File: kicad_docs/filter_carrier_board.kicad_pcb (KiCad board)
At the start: 2 copper layers, 58.4 x 99.1 mm, 30 parts, among them J1 cv_in, J10 PJ301M-12, J2 signal_in, J3 signal_out, J4 power_and_rez_cv_in, J5 PJ301M-12, J6 PJ301M-12, J7 PJ301M-12, J8 PJ301M-12, J9 power_in, U1 TL072

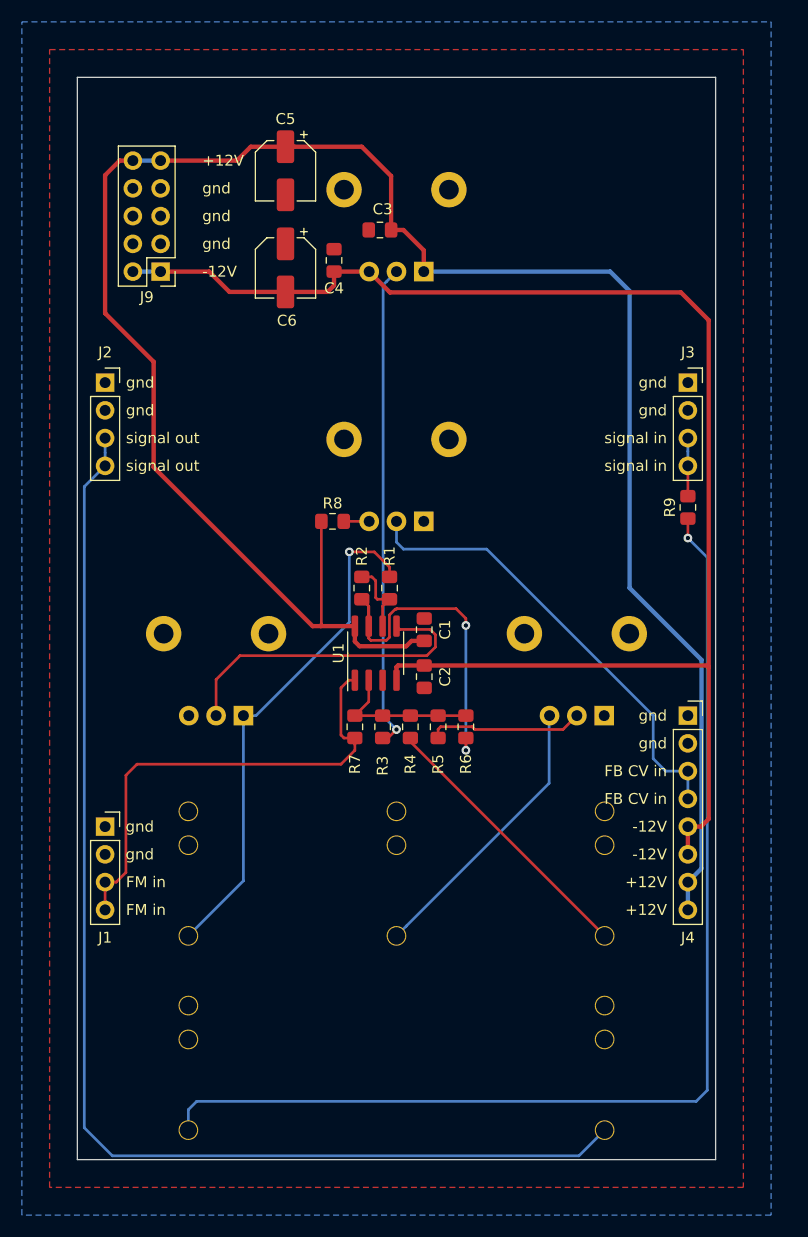
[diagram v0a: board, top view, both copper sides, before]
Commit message: route pcb traces away from pot footprints
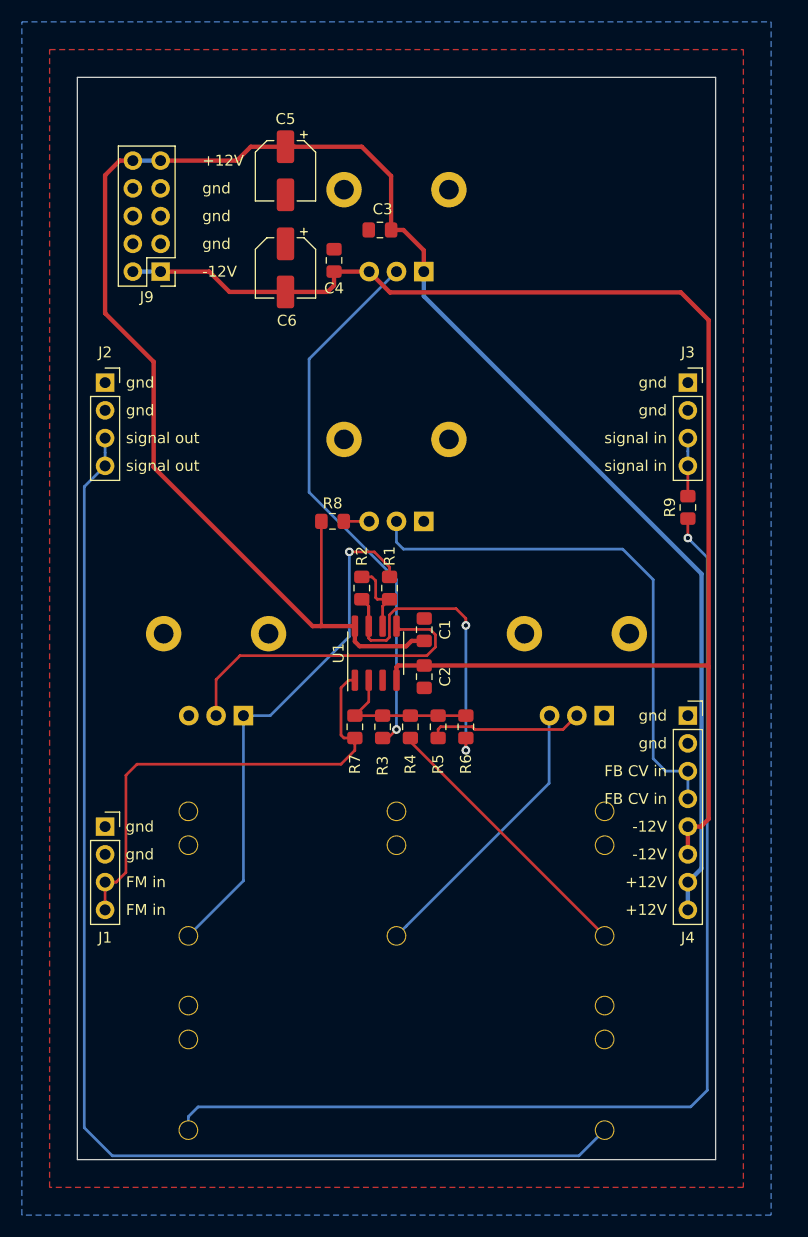
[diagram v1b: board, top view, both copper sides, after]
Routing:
- net +12V: track 191.1 -> 181.1 mm
- net Net-(J4-Pad3): track 42.1 -> 49.4 mm
- net Net-(R3-Pad2): track 44.5 -> 50.1 mm
- net Net-(J8-Pad3): track 47.1 -> 47.8 mm
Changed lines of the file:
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@@
     (thickness 1.6)
     (drawings 44)
-    (tracks 161)
+    (tracks 159)
     (zones 0)
     (modules 30)
@@
   (segment (start 105.41 68.58) (end 109.855 73.025) (width 0.4) (layer F.Cu) (net 1))
   (segment (start 109.855 82.677) (end 124.398 97.22) (width 0.4) (layer F.Cu) (net 1))
-  (segment (start 153.416 66.548) (end 151.638 64.77) (width 0.4) (layer B.Cu) (net 1))
-  (segment (start 153.416 93.726) (end 153.416 66.548) (width 0.4) (layer B.Cu) (net 1))
-  (segment (start 151.638 64.77) (end 134.58 64.77) (width 0.4) (layer B.Cu) (net 1))
-  (segment (start 160.000001 100.310001) (end 153.416 93.726) (width 0.4) (layer B.Cu) (net 1))
+  (segment (start 134.58 67.016) (end 134.58 64.77) (width 0.4) (layer B.Cu) (net 1))
+  (segment (start 160.000001 92.436001) (end 134.58 67.016) (width 0.4) (layer B.Cu) (net 1))
   (segment (start 158.75 120.65) (end 160.000001 119.399999) (width 0.4) (layer B.Cu) (net 1))
-  (segment (start 160.000001 119.399999) (end 160.000001 100.310001) (width 0.4) (layer B.Cu) (net 1))
+  (segment (start 160.000001 119.399999) (end 160.000001 92.436001) (width 0.4) (layer B.Cu) (net 1))
   (segment (start 158.75 118.11) (end 158.75 115.57) (width 0.4) (layer F.Cu) (net 3))
   (segment (start 158.75 115.57) (end 159.952081 115.57) (width 0.4) (layer F.Cu) (net 3))
@@
   (via (at 158.75 89.154) (size 0.8) (drill 0.4) (layers F.Cu B.Cu) (net 6))
   (segment (start 158.75 87.376) (end 158.75 89.154) (width 0.25) (layer F.Cu) (net 6))
-  (segment (start 159.512 140.716) (end 113.792 140.716) (width 0.25) (layer B.Cu) (net 6))
-  (segment (start 160.525011 139.702989) (end 159.512 140.716) (width 0.25) (layer B.Cu) (net 6))
-  (segment (start 113.792 140.716) (end 113.03 141.478) (width 0.25) (layer B.Cu) (net 6))
+  (segment (start 113.03 142.113) (end 113.03 143.35) (width 0.25) (layer B.Cu) (net 6))
+  (segment (start 159.004 141.224) (end 113.919 141.224) (width 0.25) (layer B.Cu) (net 6))
+  (segment (start 113.919 141.224) (end 113.03 142.113) (width 0.25) (layer B.Cu) (net 6))
+  (segment (start 160.525011 139.702989) (end 159.004 141.224) (width 0.25) (layer B.Cu) (net 6))
   (segment (start 158.75 89.154) (end 160.525011 90.929011) (width 0.25) (layer B.Cu) (net 6))
-  (segment (start 113.03 141.478) (end 113.03 143.35) (width 0.25) (layer B.Cu) (net 6))
   (segment (start 160.525011 90.929011) (end 160.525011 139.702989) (width 0.25) (layer B.Cu) (net 6))
-  (segment (start 158.75 81.212081) (end 158.75 82.55) (width 0.25) (layer B.Cu) (net 19))
-  (segment (start 158.75 80.01) (end 158.75 81.212081) (width 0.25) (layer B.Cu) (net 19))
   (segment (start 158.75 113.03) (end 158.75 110.49) (width 0.25) (layer B.Cu) (net 7))
+  (segment (start 132.08 89.535) (end 132.715 90.17) (width 0.25) (layer B.Cu) (net 7))
   (segment (start 156.718 110.49) (end 158.75 110.49) (width 0.25) (layer B.Cu) (net 7))
-  (segment (start 132.08 89.535) (end 132.715 90.17) (width 0.25) (layer B.Cu) (net 7))
   (segment (start 132.08 87.63) (end 132.08 89.535) (width 0.25) (layer B.Cu) (net 7))
-  (segment (start 155.575 105.41) (end 155.575 109.347) (width 0.25) (layer B.Cu) (net 7))
-  (segment (start 132.715 90.17) (end 140.335 90.17) (width 0.25) (layer B.Cu) (net 7))
-  (segment (start 140.335 90.17) (end 155.575 105.41) (width 0.25) (layer B.Cu) (net 7))
+  (segment (start 132.715 90.17) (end 152.781 90.17) (width 0.25) (layer B.Cu) (net 7))
+  (segment (start 155.575 92.964) (end 155.575 109.347) (width 0.25) (layer B.Cu) (net 7))
+  (segment (start 152.781 90.17) (end 155.575 92.964) (width 0.25) (layer B.Cu) (net 7))
   (segment (start 155.575 109.347) (end 156.718 110.49) (width 0.25) (layer B.Cu) (net 7))
   (segment (start 133.35 107.79) (end 133.35 107.46) (width 0.25) (layer F.Cu) (net 8))
@@
   (segment (start 118.07 120.53) (end 113.03 125.57) (width 0.25) (layer B.Cu) (net 10))
   (segment (start 118.07 105.41) (end 118.07 120.53) (width 0.25) (layer B.Cu) (net 10))
-  (segment (start 119.22 105.41) (end 118.07 105.41) (width 0.25) (layer B.Cu) (net 10))
-  (segment (start 127.762 96.868) (end 119.22 105.41) (width 0.25) (layer B.Cu) (net 10))
-  (segment (start 127.762 90.424) (end 127.762 96.868) (width 0.25) (layer B.Cu) (net 10))
   (via (at 127.762 90.424) (size 0.8) (drill 0.4) (layers F.Cu B.Cu) (net 10))
   (segment (start 130.048 90.424) (end 127.762 90.424) (width 0.25) (layer F.Cu) (net 10))
   (segment (start 131.445 92.71) (end 131.445 91.821) (width 0.25) (layer F.Cu) (net 10))
   (segment (start 131.445 91.821) (end 130.048 90.424) (width 0.25) (layer F.Cu) (net 10))
+  (segment (start 120.523 105.41) (end 118.07 105.41) (width 0.25) (layer B.Cu) (net 10))
+  (segment (start 127.762 90.424) (end 127.762 98.171) (width 0.25) (layer B.Cu) (net 10))
+  (segment (start 127.762 98.171) (end 120.523 105.41) (width 0.25) (layer B.Cu) (net 10))
   (segment (start 130.81 95.395) (end 131.445 94.76) (width 0.25) (layer F.Cu) (net 12))
   (segment (start 130.81 97.22) (end 130.81 95.395) (width 0.25) (layer F.Cu) (net 12))
@@
   (segment (start 137.52999 95.61999) (end 132.12002 95.61999) (width 0.25) (layer F.Cu) (net 13))
   (segment (start 132.12002 95.61999) (end 132.08 95.66001) (width 0.25) (layer F.Cu) (net 13))
+  (segment (start 131.3 107.46) (end 132.08 106.68) (width 0.25) (layer F.Cu) (net 14))
+  (segment (start 130.81 107.46) (end 131.3 107.46) (width 0.25) (layer F.Cu) (net 14))
   (via (at 132.08 106.68) (size 0.8) (drill 0.4) (layers F.Cu B.Cu) (net 14))
-  (segment (start 130.81 107.46) (end 131.3 107.46) (width 0.25) (layer F.Cu) (net 14))
-  (segment (start 131.3 107.46) (end 132.08 106.68) (width 0.25) (layer F.Cu) (net 14))
-  (segment (start 131.180001 65.669999) (end 132.08 64.77) (width 0.25) (layer B.Cu) (net 14))
-  (segment (start 130.854999 65.995001) (end 131.180001 65.669999) (width 0.25) (layer B.Cu) (net 14))
-  (segment (start 130.854999 105.454999) (end 130.854999 65.995001) (width 0.25) (layer B.Cu) (net 14))
-  (segment (start 132.08 106.68) (end 130.854999 105.454999) (width 0.25) (layer B.Cu) (net 14))
+  (segment (start 124.079 72.771) (end 132.08 64.77) (width 0.25) (layer B.Cu) (net 14))
+  (segment (start 124.079 84.963) (end 124.079 72.771) (width 0.25) (layer B.Cu) (net 14))
+  (segment (start 132.08 106.68) (end 132.08 92.964) (width 0.25) (layer B.Cu) (net 14))
+  (segment (start 132.08 92.964) (end 124.079 84.963) (width 0.25) (layer B.Cu) (net 14))
   (segment (start 130.81 105.41) (end 138.43 105.41) (width 0.25) (layer F.Cu) (net 15))
   (segment (start 130.81 105.41) (end 128.27 105.41) (width 0.25) (layer F.Cu) (net 15))
@@
   (segment (start 135.15819 97.52) (end 135.64501 98.00682) (width 0.25) (layer F.Cu) (net 18))
   (segment (start 134.8582 99.91999) (end 117.75801 99.91999) (width 0.25) (layer F.Cu) (net 18))
+  (segment (start 158.75 81.212081) (end 158.75 82.55) (width 0.25) (layer B.Cu) (net 19))
+  (segment (start 158.75 80.01) (end 158.75 81.212081) (width 0.25) (layer B.Cu) (net 19))
   (segment (start 158.75 85.326) (end 158.75 82.55) (width 0.25) (layer F.Cu) (net 19))
   (zone (net 2) (net_name GND) (layer B.Cu) (hatch edge 0.508)

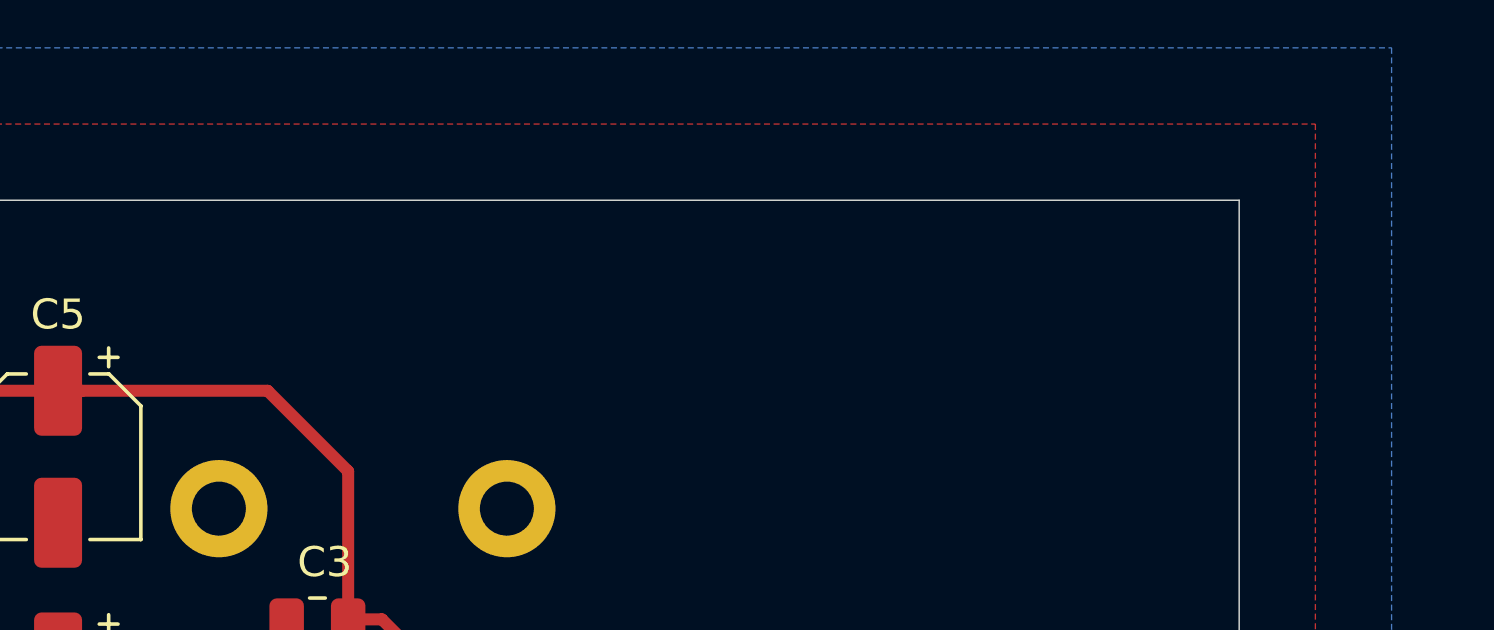
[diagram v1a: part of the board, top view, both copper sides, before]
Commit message: add github url to pcb silkscreen
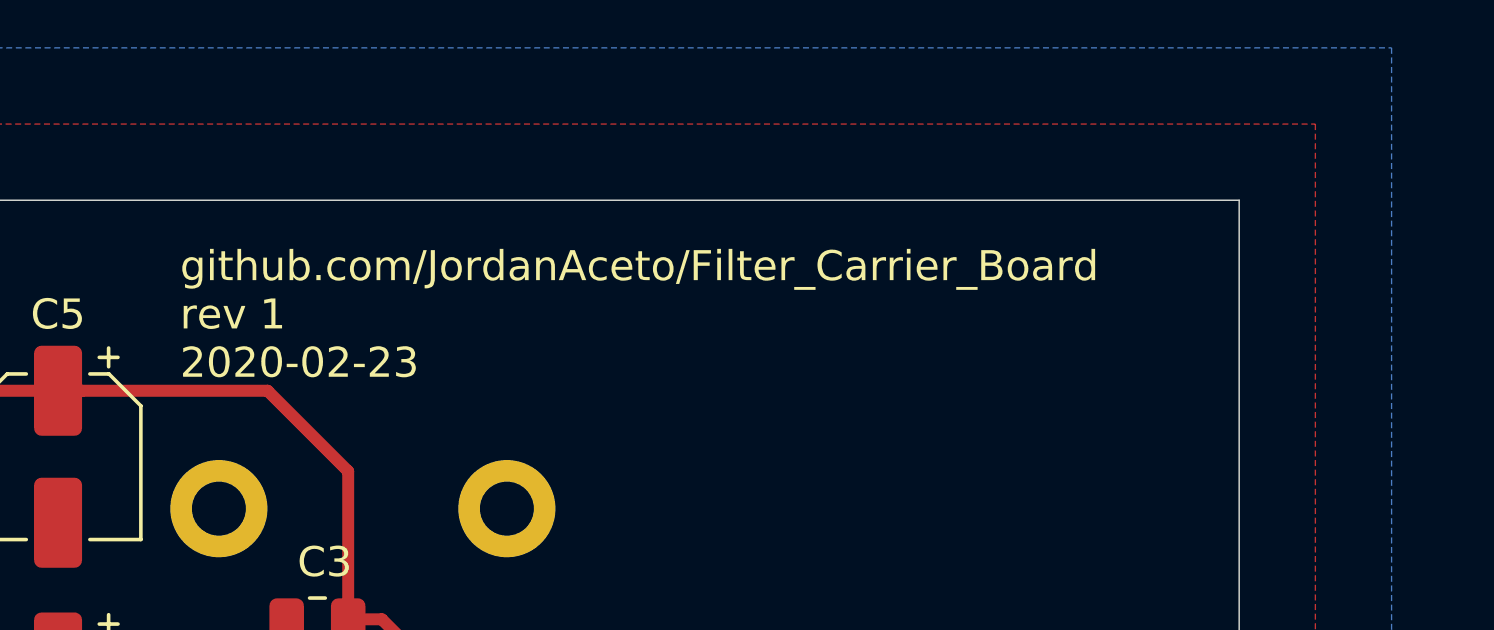
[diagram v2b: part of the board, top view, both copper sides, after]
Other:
- board text added: "github.com/JordanAceto/Filter_Carrier_Board rev 1 2020-02-23"
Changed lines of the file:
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@@
   (general
     (thickness 1.6)
-    (drawings 44)
+    (drawings 45)
     (tracks 159)
     (zones 0)
@@
     )
   )
+  (gr_text "github.com/JordanAceto/Filter_Carrier_Board\nrev 1\n2020-02-23" (at 125.984 50.8) (layer F.SilkS)
+    (effects (font (size 1 1) (thickness 0.15)) (justify left))
+  )
   (gr_text -12V (at 111.76 64.77) (layer B.SilkS)

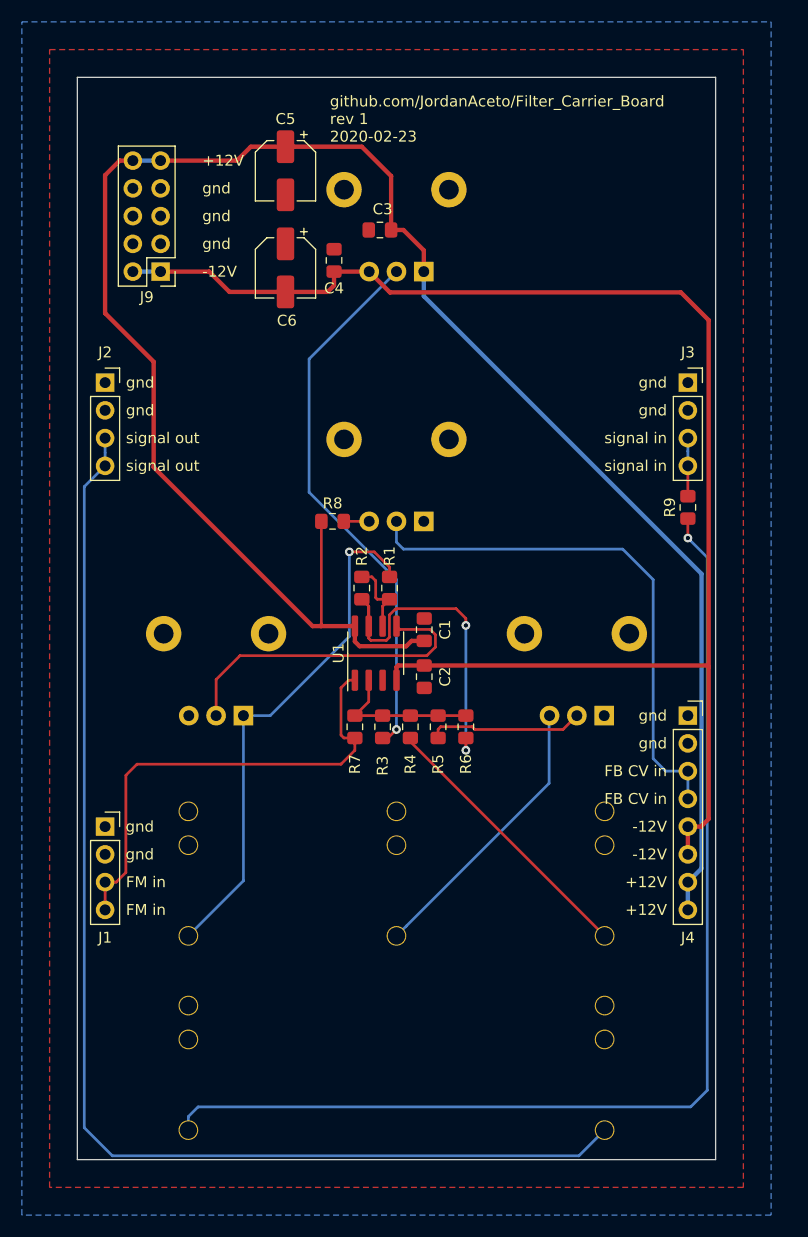
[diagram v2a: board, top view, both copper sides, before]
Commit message: invert CV to proper polarity
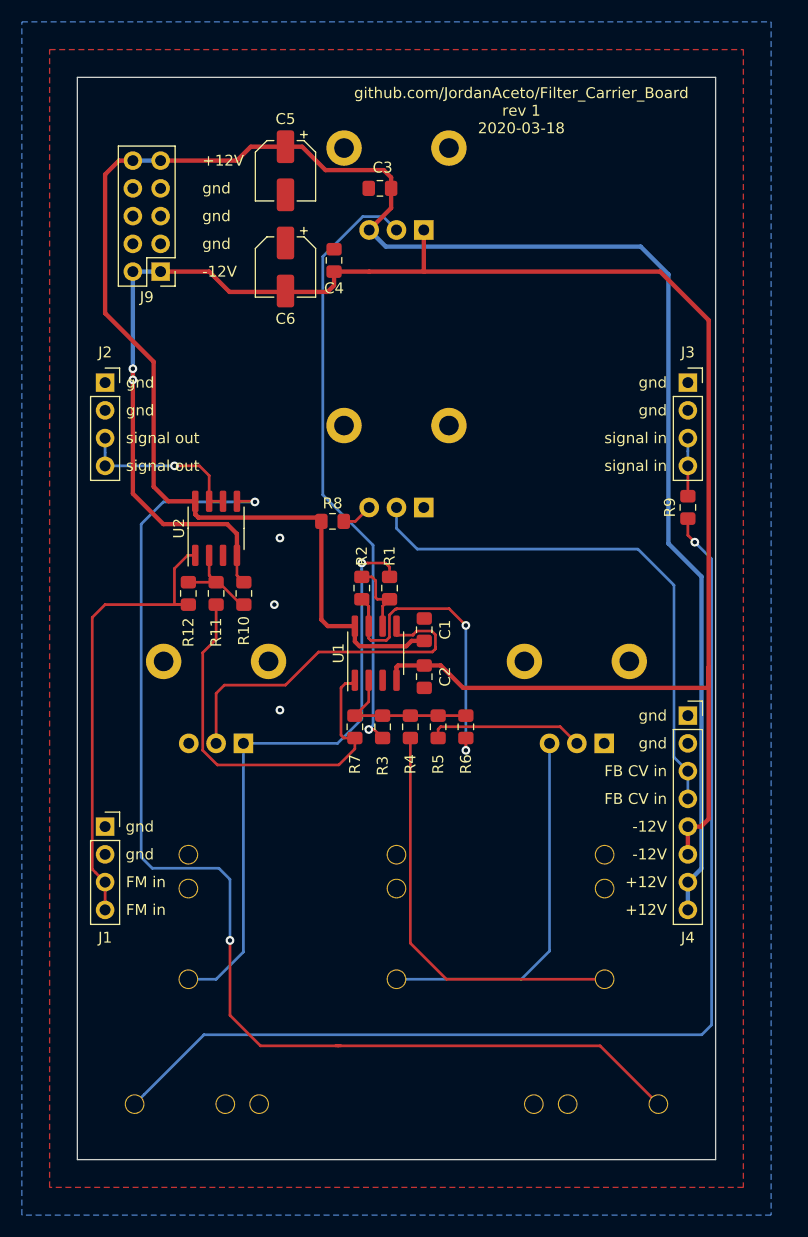
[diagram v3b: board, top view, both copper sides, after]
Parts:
- added R10: 240k, Resistor_SMD:R_0805_2012Metric_Pad1.15x1.40mm_HandSolder, F.Cu at (118.1, 94.2)
- added R11: 22k, Resistor_SMD:R_0805_2012Metric_Pad1.15x1.40mm_HandSolder, F.Cu at (115.6, 94.2)
- added R12: 22k, Resistor_SMD:R_0805_2012Metric_Pad1.15x1.40mm_HandSolder, F.Cu at (113.0, 94.2)
- added U2: TL072, Package_SO:SOIC-8_3.9x4.9mm_P1.27mm, F.Cu at (115.6, 88.3)
- R7: value 20k -> 22k
- moved J6 3.97 mm to (151.1, 124.6)
- moved J7 3.97 mm to (132.1, 124.6)
- moved J8 3.97 mm to (113.0, 124.6)
- moved C3 3.81 mm to (130.6, 57.1)
- moved RV1 3.81 mm to (134.6, 61.0)
- moved RV2 2.54 mm to (151.1, 108.0)
- moved RV3 2.54 mm to (118.1, 108.0)
- moved J10 2.54 mm to (113.0, 141.0), turned to 270 degrees
- moved J5 2.54 mm to (151.1, 141.0), turned to 90 degrees
- moved RV4 1.27 mm to (134.6, 86.4)
- moved C6 0.08 mm to (121.9, 64.3)
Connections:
- J5 pad 3: Net-(J2-Pad3) -> Net-(J5-Pad3)
- R7 pad 1: Net-(J1-Pad3) -> Net-(R11-Pad2)
- RV1 pad 1: +12V -> -12V
- RV1 pad 3: -12V -> +12V
- U1 pad 1: Net-(J1-Pad3) -> Net-(R11-Pad2)
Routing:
- net Net-(J5-Pad3): track 0.00 -> 107.9 mm, vias 0 -> 2
- net Net-(J2-Pad3): track 113.6 -> 16.1 mm, vias 0 -> 1
- net -12V: track 137.1 -> 180.6 mm, vias 0 -> 2
- net Net-(R11-Pad2): track 0.00 -> 37.2 mm
- net Net-(J6-Pad3): track 25.5 -> 37.9 mm
- net +12V: track 181.1 -> 191.3 mm
- net Net-(R10-Pad1): track 0.00 -> 8.65 mm
- net Net-(J7-Pad3): track 26.0 -> 34.1 mm
- net Net-(J8-Pad3): track 47.8 -> 54.8 mm
- net Net-(R3-Pad2): track 50.1 -> 56.8 mm
- net Net-(RV3-Pad2): track 29.6 -> 32.3 mm
- net Net-(J1-Pad3): track 44.0 -> 42.8 mm
- net Net-(R8-Pad2): track 2.33 -> 2.85 mm
- net GND: vias 0 -> 3
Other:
- board text added: "github.com/JordanAceto/Filter_Carrier_Board rev 1 2020-03-18"
- board text removed: "github.com/JordanAceto/Filter_Carrier_Board rev 1 2020-02-23"
